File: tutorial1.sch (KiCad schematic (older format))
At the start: 9 parts, among them IC1 PIC12C508A-I/SN, J1 MYCONN3, P1 USB_OTG, P2 USB_OTG, P3 USB_OTG

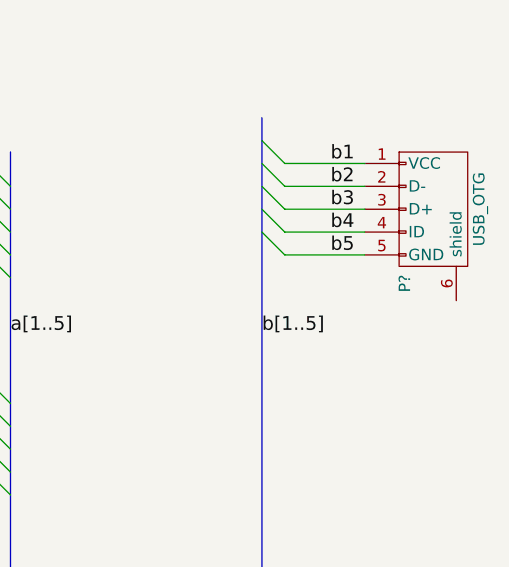
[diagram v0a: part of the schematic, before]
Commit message: changed J1 footprint to Molex
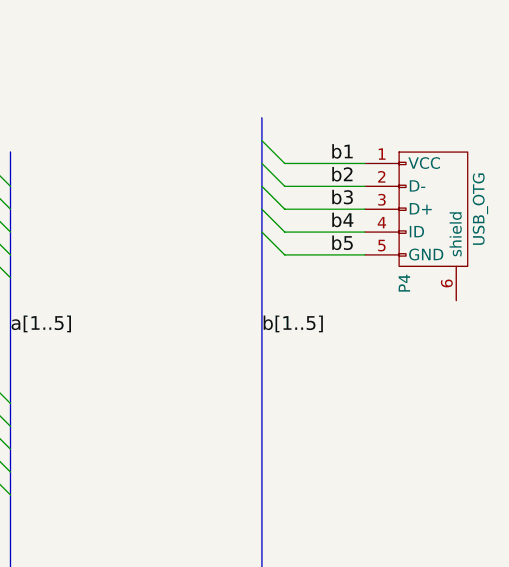
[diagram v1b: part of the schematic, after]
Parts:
- J1: footprint Connect:Banana_Jack_3Pin -> Connectors_Molex:Molex_KK-6410-03_03x2.54mm_Straight
- gave numbers to parts that had none: 1
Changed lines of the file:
@@
 F 0 "J1" H 3000 2400 60  0000 C CNN
 F 1 "MYCONN3" H 3000 2800 60  0000 C CNN
-F 2 "Connect:Banana_Jack_3Pin" H 3000 2800 60  0001 C CNN
+F 2 "Connectors_Molex:Molex_KK-6410-03_03x2.54mm_Straight" H 3000 2800 60  0001 C CNN
 F 3 "" H 3000 2800 60  0000 C CNN
 	1    3000 2800
@@
 a[1..5]
 $Comp
-L USB_OTG P?
+L USB_OTG P4
 U 1 1 59AF0BD4
 P 5600 4450
-F 0 "P?" H 5925 4325 50  0000 C CNN
+F 0 "P4" H 5925 4325 50  0000 C CNN
 F 1 "USB_OTG" H 5600 4650 50  0000 C CNN
 F 2 "" V 5550 4350 50  0000 C CNN
